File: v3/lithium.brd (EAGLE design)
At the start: 74.3 x 54.6 mm, 32 parts, among them U1 TPS61088VQFN20, U2 TPS63051RMW, U3 SI2301BDS-T1-E3, U4 TPS2113APWR

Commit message: Significant completion of scheamtic.
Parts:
- removed U$2: MCP73833-FCI/UN, 32bits:MSOP10_MC
- added BATT, USB: 597-3311-407F, Dialight_By_element14_Batch_1:LED_597-3311-407F
- added C1, C2: 1.0uF, SparkFun-Capacitors:0402
- added C3, C4: 0.1uF, SparkFun-Capacitors:0402
- added CHG: 597-3111-407F, Dialight_By_element14_Batch_1:LED_597-3111-407F
- added DONE: 597-3401-407F, Dialight_By_element14_Batch_1:LED_597-3401-407F
- added J1: batt, SparkFun-Connectors:JST-2-SMD
- added R3: 10K Ohms, Vishay_By_element14_Batch_1:RESC1005X40N
- added R4: 1K Ohm, Vishay_By_element14_Batch_1:RESC1005X40N
- added R5, R6, R7: 100 Ohms, Yageo_By_element14_Batch_1:RESC1005X40N
- added R8: 22, SparkFun-Resistors:0402
- added R9: 200 Ohms, Vishay_By_element14_Batch_1:RESC3216X71N
- added RPG1: 100K Ohms, Vishay_By_element14_Batch_1:RESC1608X60N
- added S1: AS11CH, 32bits:AS11CH
- added U5: MCP73833-FCI/UN, 32bits:MSOP10_MC
- J3: value (none) -> robo
- moved U4 192.0 mm to (63.5, 33.0)
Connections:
- removed net VIN: CIN.2, CIN1.2, CIN2.2, L1.2, U1.P$9, U2.P$10, U2.P$12
- new net N$10: BATT.2, R9.1
- new net N$11: S1.P$1, U4.7
- new net N$2: R8.2, U4.4
- new net N$5: R4.1, U5.6
- new net N$6: R3.1, U5.8
- new net N$7: CHG.2, R5.1
- new net N$8: DONE.2, R6.1
- new net N$9: R7.1, USB.2
- new net STAT: BATT.1, RPG1.2, U4.1
- new net STAT1: CHG.1, U5.3
- new net STAT2: DONE.1, U5.4
- new net U5_NPG: U5.7, USB.1
- new net VBAT: C2.1, C4.1, J1.2, U4.8, U5.10, U5.9
- new net VCC: CIN.2, CIN1.2, CIN2.2, L1.2, R9.2, RPG1.1, S1.P$2, U1.P$9, U2.P$10, U2.P$12
- new net VUSB: C1.1, C3.1, R5.2, R6.2, R7.2, U4.6, U5.1, U5.2
- net GND: now also C1.2, C2.2, C3.2, C4.2, J1.1, R3.2, R4.2, R8.1, U4.2, U4.3, U5.5

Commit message: Lego module mechanical and 5v rail
Switching to a 5v supply from the 3.3. Will use an LDO on the motor board to get 3.3. from the 5.
In-general, committing to a BB green/ROS controller for this robot.
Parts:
- removed CIN1, COUT1, COUTX: 10uF, Murata_By_element14_Batch_1:CAPC1608X85N
- removed CSS: 1.3nF, Kemet_By_element14_Batch_1:CAPC1005X60N
- removed J3: robo, SparkFun-Connectors:2X10
- removed RPG: 100K Ohms, Vishay_By_element14_Batch_1:RESC1608X60N
- removed U$1: BEAGLEBONE_HEADERS, 32bits:23X3X2
- removed U2: TPS63051RMW, 32bits:RMW12
- added C5: 10 nF, Kemet_By_element14_Batch_1:CAPC1005X60N
- added C6: 0.22µF, AVX_By_element14_Batch_1:CAPC1608X90N
- added P8-1-2: bb-extra-gnd, SparkFun-Connectors:1X02
- added P8-27-46: robo, SparkFun-Connectors:2X10
- added P9-1-10: bb-pwr, SparkFun-Connectors:2X5
- added P9-39-46: bb-extra-gnd, SparkFun-Connectors:2X4
- added U6: TPS61230A, 32bits:VQFN7
- L2: value AISC-1008-1R5J-T -> 1.0 uH; device 32bits:AISC-1008 -> Bourns_By_element14_Batch_1:INDC3225X22N
- S1: value AS11CH -> PWR; device 32bits:AS11CH -> 32bits:AS11CH-TOP
- moved RPG1 313.1 mm to (36.8, 15.2)
- moved R9 292.5 mm to (33.7, 5.08), flipped to the bottom, turned to 90 degrees
- moved BATT 282.1 mm to (33.7, 5.08), turned to 270 degrees
- moved USB 247.5 mm to (37.5, 5.08), turned to 270 degrees
- moved DONE 219.6 mm to (47.0, 5.08), turned to 270 degrees
- moved CHG 208.9 mm to (43.2, 5.08), turned to 270 degrees
- moved L2 172.4 mm to (-15.2, -273.1)
- moved +3.3 125.6 mm to (24.1, 5.08), turned to 270 degrees
- moved +6 61.9 mm to (27.9, 5.08), turned to 270 degrees
- moved J1 56.5 mm to (81.9, 27.3), turned to 270 degrees
- moved R1 54.6 mm to (27.9, 5.08), flipped to the bottom, turned to 90 degrees
- moved 3 48.3 mm to (74.9, 40.6)
- moved U4 20.5 mm to (61.0, 12.7)
- moved U5 20.5 mm to (68.6, 27.9)
- moved U1 19.2 mm to (29.2, 22.9)
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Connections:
- net LED_ANODE renamed LA_6
- net N$10 renamed LA_BATT
- net N$4 renamed LA_3_3
- net N$7 renamed LA_CHG
- net N$8 renamed LA_DONE
- net N$9 renamed LA_USB
- removed net L1: L2.2, U2.P$1
- removed net L2: L2.1, U2.P$3
- removed net SS1: CSS.2, U2.P$7
- new net N$4: C5.1, U6.P$1
- new net N$7: C5.2, L2.1, U6.P$5
- new net N$8: L2.2, U6.P$2, U6.P$4
- new net VOUT: U6.P$7
- net +3.3: now also P8-27-46.3, P8-27-46.4, P9-1-10.3, P9-1-10.4; no longer COUT1.2, COUTX.2, RPG.1, U2.P$4, U2.P$5
- net +6: now also P8-27-46.5, P8-27-46.6
- net EN: no longer U2.P$11
- net GND: now also P8-1-2.1, P8-1-2.2, P8-27-46.1, P8-27-46.2, P9-1-10.1, P9-1-10.2, P9-39-46.5, P9-39-46.6, P9-39-46.7, P9-39-46.8, U6.P$6; no longer CIN1.1, COUT1.1, COUTX.1, CSS.1, U2.P$2, U2.P$6, U2.P$9
- net NPG: no longer RPG.2, U2.P$8
- net VCC: no longer CIN1.2, U2.P$10, U2.P$12
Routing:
- net LA_BATT: track 0.00 -> 4.52 mm, vias 0 -> 1
- net LA_6: track 0.00 -> 3.39 mm, vias 0 -> 1
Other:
- outline, holes or cut-outs redrawn

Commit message: Progress on Lithium board.
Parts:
- removed +3.3: 597-3311-407F, Dialight_By_element14_Batch_1:LED_597-3311-407F
- removed +6: 597-3311-402F, Dialight_By_element14_Batch_1:LED_597-3311-402F
- removed C1, C2: 1.0uF, SparkFun-Capacitors:0402
- removed C22: 8.2nF, Kemet_By_element14_Batch_1:CAPC1005X60N
- removed C3, C4: 0.1uF, SparkFun-Capacitors:0402
- removed C5: 10 nF, Kemet_By_element14_Batch_1:CAPC1005X60N
- removed C6: 0.22µF, AVX_By_element14_Batch_1:CAPC1608X90N
- removed CBST: 100nF, AVX_By_element14_Batch_1:CAPC2013X94N
- removed CCOMP: 680PF, AVX_By_element14_Batch_1:CAPC1608X90N
- removed CCOMP2: 36pF, Kemet_By_element14_Batch_1:CAPC1005X60N
- removed CIN, COUT: 0.47uF, Kemet_By_element14_Batch_1:CAPC3216X180N
- removed CIN2: 100nF, Murata_By_element14_Batch_1:CAPC1005X60N
- removed CVCC: 1uF, Murata_By_element14_Batch_1:CAPC1608X85N
- removed J1: batt, SparkFun-Connectors:JST-2-SMD
- removed L1: DR73-1R0-R, Coiltronics_By_element14_Batch_1:INDM7676X355N
- removed R7: 100 Ohms, Yageo_By_element14_Batch_1:RESC1005X40N
- removed R8: 22, SparkFun-Resistors:0402
- removed R9: 200 Ohms, Vishay_By_element14_Batch_1:RESC3216X71N
- removed RCOMP: 38.3K Ohms, Vishay_By_element14_Batch_1:RESC1005X40N
- removed RFBB: 118K Ohms, Vishay_By_element14_Batch_1:RESC1005X40N
- removed RFBT: 470K Ohms, Yageo_By_element14_Batch_1:RESC1608X60N
- removed RLIM: 102K Ohms, Vishay_By_element14_Batch_1:RESC1005X40N
- removed RPG1: 100K Ohms, Vishay_By_element14_Batch_1:RESC1608X60N
- removed RT: 261K Ohms, Vishay_By_element14_Batch_1:RESC1005X40N
- removed U3: SI2301BDS-T1-E3, Vishay_By_element14_Batch_1:SOT95P237X112-3N
- added 5V: QTLP650C-4, Dialight_By_element14_Batch_1:LED_597-3311-407F
- added MOTORS: QTLP650C-B, Dialight_By_element14_Batch_1:LED_597-3311-402F
- added U1_C22: 8.2nF, Kemet_By_element14_Batch_1:CAPC1005X60N
- added U1_CBST: 100nF, AVX_By_element14_Batch_1:CAPC2013X94N
- added U1_CCOMP: 680PF, AVX_By_element14_Batch_1:CAPC1608X90N
- added U1_CCOMP2: 36pF, Kemet_By_element14_Batch_1:CAPC1005X60N
- added U1_CIN, U1_COUT: 0.47uF, Kemet_By_element14_Batch_1:CAPC3216X180N
- added U1_CIN2: 100nF, Murata_By_element14_Batch_1:CAPC1005X60N
- added U1_CVCC: 1uF, Murata_By_element14_Batch_1:CAPC1608X85N
- added U1_L1: DR73-1R0-R, Coiltronics_By_element14_Batch_1:INDM7676X355N
- added U1_RCOMP: 38.3K Ohms, Vishay_By_element14_Batch_1:RESC1005X40N
- added U1_RFBB: 118K Ohms, Vishay_By_element14_Batch_1:RESC1005X40N
- added U1_RFBT: 470K Ohms, Yageo_By_element14_Batch_1:RESC1608X60N
- added U1_RLIM: 102K Ohms, Vishay_By_element14_Batch_1:RESC1005X40N
- added U1_RT: 261K Ohms, Vishay_By_element14_Batch_1:RESC1005X40N
- added U4_C3, U4_C4: 0.1uF, SparkFun-Capacitors:0402
- added U4_R8: 22, SparkFun-Resistors:0402
- added U4_RPG: 100K Ohms, Vishay_By_element14_Batch_1:RESC1608X60N
- added U5_C1, U5_C2: 1.0uF, SparkFun-Capacitors:0402
- added U5_R1: 1K Ohm, Vishay_By_element14_Batch_1:RESC1005X40N
- added U5_R2: 10K Ohms, Vishay_By_element14_Batch_1:RESC3216X71N
- added U6_CBST: 10 nF, Kemet_By_element14_Batch_1:CAPC1005X60N
- added U6_CFF: 10pF, Kemet_By_element14_Batch_1:CAPC1608X85N
- added U6_CIN: 22uF, Murata_By_element14_Batch_1:CAPC2013X135N
- added U6_COUT: 22uF, Murata_By_element14_Batch_1:CAPC3225X270N
- added U6_RFBB: 100K Ohms, Vishay_By_element14_Batch_1:RESC1005X40N
- added U6_RFBT: 316K Ohms, Vishay_By_element14_Batch_1:RESC1005X40N
- BATT, USB: value 597-3311-407F -> QTLP650C-4
- CHG: value 597-3111-407F -> QTLP650C-7
- DONE: value 597-3401-407F -> QTLP650C-3
- P8-27-46: value robo -> motors
- R1: value 200 Ohms -> 15 Ohm; device Vishay_By_element14_Batch_1:RESC3216X71N -> Vishay_By_element14_Batch_1:RESC2013X65N
- R2, R5, R6: value 100 Ohms -> 15 Ohm; device Yageo_By_element14_Batch_1:RESC1005X40N -> Vishay_By_element14_Batch_1:RESC2013X65N
- R3: value 10K Ohms -> 15 Ohm; device Vishay_By_element14_Batch_1:RESC1005X40N -> Vishay_By_element14_Batch_1:RESC2013X65N
- R4: value 1K Ohm -> 15 Ohm; device Vishay_By_element14_Batch_1:RESC1005X40N -> Vishay_By_element14_Batch_1:RESC2013X65N
- U1: device digikey:VQFN20 -> 32bits:VQFN20
- moved L2 327.5 mm to (48.3, 48.3), turned to 90 degrees
- moved U6 318.6 mm to (39.4, 49.5)
- moved R6 237.3 mm to (33.7, 5.08), flipped to the bottom, turned to 90 degrees
- moved R5 228.0 mm to (37.5, 5.08), flipped to the bottom, turned to 90 degrees
- moved R3 195.6 mm to (24.1, 5.08), flipped to the bottom, turned to 90 degrees
- moved R4 186.3 mm to (27.9, 5.08), flipped to the bottom, turned to 90 degrees
- moved R2 135.3 mm to (47.0, 5.08), flipped to the bottom, turned to 90 degrees
- moved U1 27.3 mm to (55.2, 14.6), turned to 180 degrees
- moved CHG 19.1 mm to (24.1, 5.08)
- moved DONE 19.1 mm to (27.9, 5.08)
- moved R1 15.2 mm to (43.2, 5.08)
- moved U4 10.8 mm to (70.5, 17.8)
- moved U5 1.80 mm to (67.3, 26.7)
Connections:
- net N$11 renamed S1_U4OUT
- removed net +3.3: P8-27-46.3, P8-27-46.4, P9-1-10.3, P9-1-10.4, R2.2
- removed net +6: COUT.2, P8-27-46.5, P8-27-46.6, R1.2, RFBT.1, U1.P$14, U1.P$15, U1.P$16
- removed net COMP: CCOMP2.2, RCOMP.1, U1.P$18
- removed net EN: U1.P$2
- removed net LA_3_3: +3.3.2, R2.1
- removed net MODE: U1.P$13
- removed net N$2: R8.2, U4.4
- removed net N$3: +3.3.1, U3.3
- removed net N$5: R4.1, U5.6
- removed net N$6: R3.1, U5.8
- removed net N$8: L2.2, U6.P$2, U6.P$4
- removed net NPG: U3.1
- removed net STAT: BATT.1, RPG1.2, U4.1
- removed net VCC1: CVCC.1, U1.P$1
- removed net VOUT: U6.P$7
- new net LA_5: 5V.2, R1.1
- new net MOT_6V: P8-27-46.17, P8-27-46.18, R2.2, U1.P$14, U1.P$15, U1.P$16, U1_COUT.2, U1_RFBT.1
- new net N$9: U6.P$3, U6_CFF.1, U6_RFBB.1, U6_RFBT.2
- new net SYS_5V: P9-1-10.7, P9-1-10.8, R1.2, U6.P$7, U6_CFF.2, U6_COUT.2, U6_RFBT.1
- new net U1_COMP: U1.P$18, U1_CCOMP2.2, U1_RCOMP.1
- new net U1_VCC: U1.P$1, U1.P$2, U1_CVCC.1
- new net U4_ILIM: U4.4, U4_R8.2
- new net U4_STAT: BATT.1, U4.1, U4_RPG.2
- new net U5_PROG: U5.6, U5_R1.1
- new net U5_THERM: P8-27-46.5, U5.8, U5_R2.1
- net BOOT: now also U1_CBST.1; no longer CBST.1
- net FB: now also U1_RFBB.2, U1_RFBT.2; no longer RFBB.2, RFBT.2
- net FSW: now also U1_RT.1; no longer RT.1
- net GND: now also 5V.1, MOTORS.1, P8-27-46.15, P8-27-46.16, P8-27-46.19, P8-27-46.20, U1_C22.1, U1_CCOMP.1, U1_CCOMP2.1, U1_CIN.1, U1_CIN2.1, U1_COUT.1, U1_CVCC.2, U1_RFBB.1, U1_RLIM.2, U4_C3.2, U4_C4.2, U4_R8.1, U5_C1.2, U5_C2.2, U5_R1.2, U5_R2.2, U6_CIN.1, U6_COUT.1, U6_RFBB.2; no longer +6.1, C1.2, C2.2, C22.1, C3.2, C4.2, CCOMP.1, CCOMP2.1, CIN.1, CIN2.1, COUT.1, CVCC.2, J1.1, R3.2, R4.2, R8.1, RFBB.1, RLIM.2, U3.2
- net ILIM: now also U1_RLIM.1; no longer RLIM.1
- net LA_6: now also MOTORS.2, R2.1; no longer +6.2, R1.1
- net LA_BATT: now also R6.1; no longer R9.1
- net LA_CHG: now also R3.1; no longer R5.1
- net LA_DONE: now also R4.1; no longer R6.1
- net LA_USB: now also R5.1; no longer R7.1
- net N$1: now also U1_CCOMP.2, U1_RCOMP.2; no longer CCOMP.2, RCOMP.2
- net N$4: now also U6_CBST.1; no longer C5.1
- net N$7: now also U6_CBST.2; no longer C5.2
- net SS: now also U1_C22.2; no longer C22.2
- net SW: now also U1_CBST.2, U1_L1.1, U1_RT.2; no longer CBST.2, L1.1, RT.2
- net VBAT: now also P8-27-46.3, P8-27-46.4, U4_C4.1, U5_C2.1; no longer C2.1, C4.1, J1.2
- net VCC: now also L2.2, R6.2, U1_CIN.2, U1_CIN2.2, U1_L1.2, U4_RPG.1, U6.P$2, U6.P$4, U6_CIN.2; no longer CIN.2, CIN2.2, L1.2, R9.2, RPG1.1
- net VUSB: now also P8-27-46.13, P8-27-46.14, R3.2, R4.2, U4_C3.1, U5_C1.1; no longer C1.1, C3.1, R6.2, R7.2
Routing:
- net STAT1: track 0.00 -> 59.4 mm, vias 0 -> 2
- net STAT2: track 0.00 -> 59.2 mm, vias 0 -> 2
- net U5_NPG: track 0.00 -> 50.4 mm, vias 0 -> 2
- net VUSB: track 0.00 -> 43.4 mm
- net U5_THERM: track 0.00 -> 42.1 mm, vias 0 -> 3
- net VCC: track 0.00 -> 27.9 mm, vias 0 -> 1
- net MOT_6V: track 0.00 -> 9.28 mm, vias 0 -> 1
- net FB: track 0.00 -> 6.24 mm
- net U1_COMP: track 0.00 -> 5.79 mm
- net LA_5: track 0.00 -> 3.83 mm, vias 0 -> 1
- net LA_DONE: track 0.00 -> 3.83 mm, vias 0 -> 1
- net LA_CHG: track 0.00 -> 3.83 mm, vias 0 -> 1
- net LA_USB: track 0.00 -> 3.83 mm, vias 0 -> 1
- net BOOT: track 0.00 -> 2.14 mm
- net FSW: track 0.00 -> 1.70 mm
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- added copper zone on layer 1, net MOT_6V
- added copper zone on layer 1, net SW
- added copper zone on layer 1, net U1_VCC
- added copper zone on layer 1, net VCC
- added copper zone on layer 1, net VUSB
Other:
- board size 74.3 x 54.6 mm -> 71.8 x 54.6 mm

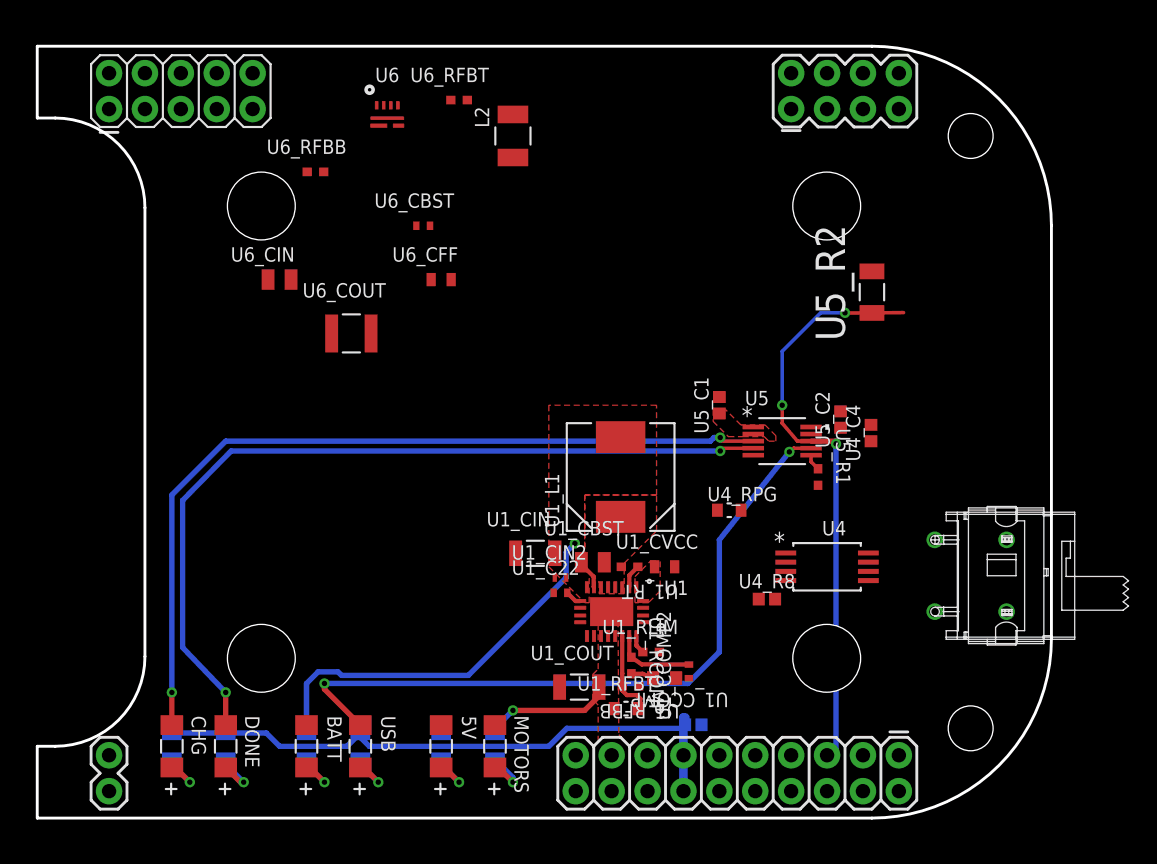
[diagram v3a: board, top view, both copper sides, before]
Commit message: Significant completion of Lithium layout.
TODO:
1. reverse voltage protection.
2. silk screen
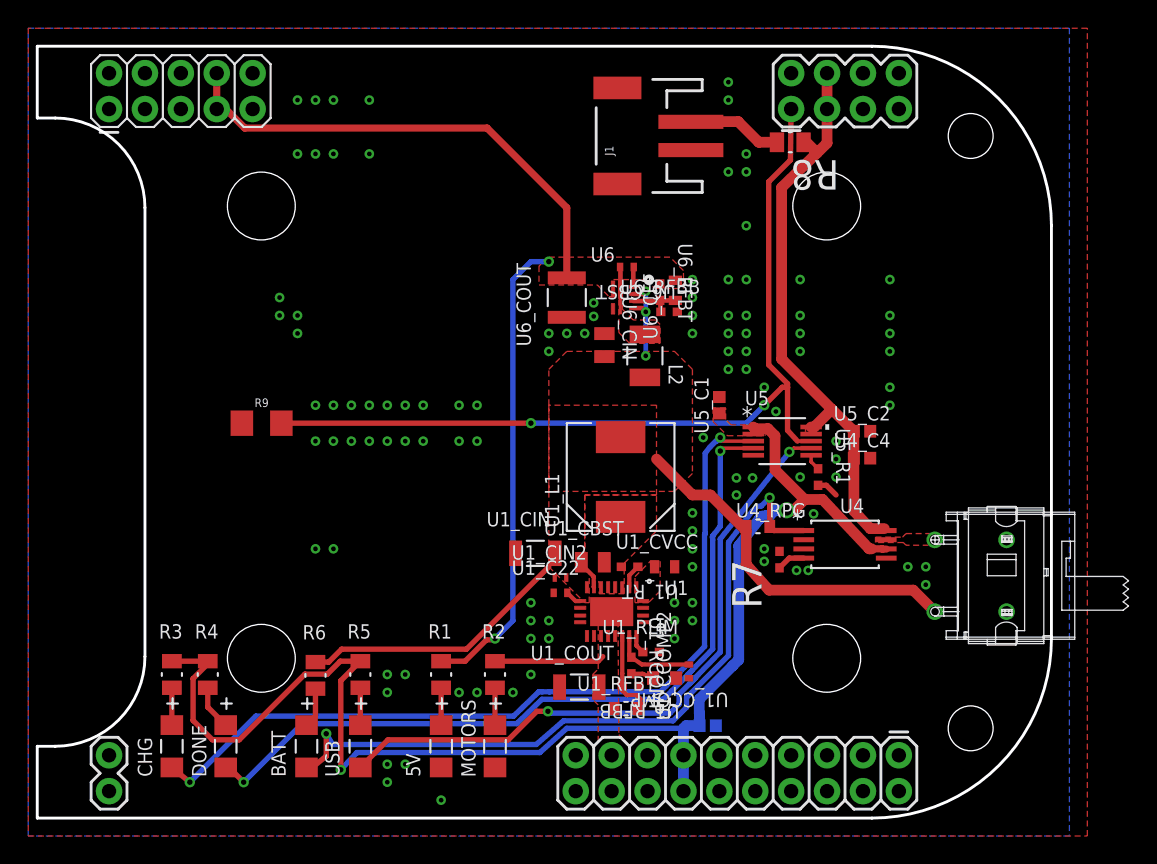
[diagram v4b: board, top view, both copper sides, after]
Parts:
- removed U4_R8: 22, SparkFun-Resistors:0402
- removed U5_R2: 10K Ohms, Vishay_By_element14_Batch_1:RESC3216X71N
- added J1: batt, SparkFun-Connectors:JST-2-SMD
- added R7: 22 Ohms, Vishay_By_element14_Batch_1:RESC1005X40N
- added R8: 0Ohm, Vishay_By_element14_Batch_1:RESC2013X65N
- added R9: 10k, 32bits:1206
- moved U6_RFBB 26.9 mm to (59.3, 35.8)
- moved U6_CIN 23.4 mm to (54.7, 33.5), turned to 270 degrees
- moved U6 20.8 mm to (55.9, 36.8), turned to 270 degrees
- moved U6_RFBT 19.7 mm to (58.7, 37.2), turned to 270 degrees
- moved L2 18.1 mm to (57.6, 32.7), turned to 270 degrees
- moved U6_CFF 16.6 mm to (59.8, 37.3), turned to 90 degrees
- moved U6_COUT 15.5 mm to (52.1, 36.8), turned to 90 degrees
- moved U6_CBST 14.7 mm to (56.3, 39.0), turned to 180 degrees
- moved R4 5.24 mm to (26.7, 10.2), flipped to the top
- moved R1 5.08 mm to (43.2, 10.2), flipped to the top
- moved R2 5.08 mm to (47.0, 10.2), flipped to the top
- moved R3 5.08 mm to (24.1, 10.2), flipped to the top
- moved R5 5.08 mm to (37.5, 10.2), flipped to the top
- moved R6 5.06 mm to (34.3, 10.1), flipped to the top
- moved U4_RPG 2.33 mm to (65.6, 20.6)
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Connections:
- net N$4 renamed U6_CBST
- net N$7 renamed U6_SW
- net N$9 renamed U6_FB
- removed net GND: 5V.1, MOTORS.1, P8-1-2.1, P8-1-2.2, P8-27-46.1, P8-27-46.15, P8-27-46.16, P8-27-46.19, P8-27-46.2, P8-27-46.20, P9-1-10.1, P9-1-10.2, P9-39-46.5, P9-39-46.6, P9-39-46.7, P9-39-46.8, U1.P$11, U1.P$12, U1.P$20, U1.P$21, U1.P$22, U1.P$23, U1.P$24, U1.P$25, U1_C22.1, U1_CCOMP.1, U1_CCOMP2.1, U1_CIN.1, U1_CIN2.1, U1_COUT.1, U1_CVCC.2, U1_RFBB.1, U1_RLIM.2, U4.2, U4.3, U4.5, U4_C3.2, U4_C4.2, U4_R8.1, U5.5, U5_C1.2, U5_C2.2, U5_R1.2, U5_R2.2, U6.P$6, U6_CIN.1, U6_COUT.1, U6_RFBB.2
- new net COPU: 5V.1, J1.1, MOTORS.1, P8-1-2.1, P8-1-2.2, P8-27-46.1, P8-27-46.15, P8-27-46.16, P8-27-46.19, P8-27-46.2, P8-27-46.20, P9-1-10.1, P9-1-10.2, P9-39-46.5, P9-39-46.6, P9-39-46.7, P9-39-46.8, R7.2, R9.1, U1.P$11, U1.P$12, U1.P$20, U1.P$21, U1.P$22, U1.P$23, U1.P$24, U1.P$25, U1_C22.1, U1_CCOMP.1, U1_CCOMP2.1, U1_CIN.1, U1_CIN2.1, U1_COUT.1, U1_CVCC.2, U1_RFBB.1, U1_RLIM.2, U4.2, U4.3, U4.5, U4_C3.2, U4_C4.2, U5.5, U5_C1.2, U5_C2.2, U5_R1.2, U6.P$6, U6_CIN.1, U6_COUT.1, U6_RFBB.2
- new net LOCAL_VBAT: J1.2, R8.2
- net S1_U4OUT: now also S1.P$2; no longer S1.P$1
- net U4_ILIM: now also R7.1; no longer U4_R8.2
- net U5_THERM: now also P9-39-46.1, R9.2; no longer P8-27-46.5, U5_R2.1
- net VBAT: now also P9-39-46.3, P9-39-46.4, R8.1; no longer P8-27-46.3, P8-27-46.4
- net VCC: now also S1.P$1; no longer S1.P$2
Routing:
- net SYS_5V: track 0.00 -> 68.6 mm, vias 0 -> 2
- net VUSB: track 43.4 -> 95.8 mm, vias 0 -> 2
- net U4_STAT: track 0.00 -> 52.1 mm, vias 0 -> 2
- net VBAT: track 0.00 -> 40.6 mm
- net VCC: track 27.9 -> 51.4 mm, vias 1 -> 3
- net U5_THERM: track 42.1 -> 62.8 mm, vias 3 -> 2
- net LOCAL_VBAT: track 0.00 -> 6.70 mm
- net U6_FB: track 0.00 -> 3.79 mm
- net STAT2: track 59.2 -> 55.5 mm
- net U5_NPG: track 50.4 -> 47.5 mm
- net U6_SW: track 0.00 -> 2.21 mm
- net U4_ILIM: track 0.00 -> 2.00 mm
- net COPU: track 0.00 -> 1.55 mm, vias 0 -> 111
- net MOT_6V: track 9.28 -> 7.76 mm, vias 1 -> 0
- net U6_CBST: track 0.00 -> 1.42 mm
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- added copper zone on layer 1, net COPU
- added copper zone on layer 16, net COPU
- added copper zone on layer 1, net S1_U4OUT
- added copper zone on layer 1, net SYS_5V
- added copper zone on layer 1, net U6_SW
- added copper zone on layer 1, net VBAT
